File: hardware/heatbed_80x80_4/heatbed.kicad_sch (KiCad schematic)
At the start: 1 part, among them J1 PWR

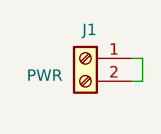
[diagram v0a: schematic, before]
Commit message: Increase holes' diameters
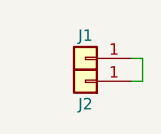
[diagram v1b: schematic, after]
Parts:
- removed J1: PWR, Connector_PinHeader_2.54mm:PinHeader_1x02_P2.54mm_Vertical, symbol Connector:Screw_Terminal_01x02
- added J1, J2: Conn_01x01, Connector_Pin:Pin_D1.3mm_L11.0mm, symbol Connector_Generic:Conn_01x01
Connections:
- new net: J1.1 (Pin_1), J2.1 (Pin_1)
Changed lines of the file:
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@@
     (stroke (width 0) (type default))
   )
-  (symbol (lib_id "Connector:Screw_Terminal_01x02") (at 147.32 100.33 0) (mirror y) (unit 1)
-    (in_bom yes) (on_board yes) (dnp no)
-    (property "Reference" "J1" (at 148.59 97.155 0)
-      (effects (font (size 1.27 1.27)) (justify left))
+  (symbol (lib_id "Connector_Generic:Conn_01x01") (at 147.32 100.33 180) (unit 1)
+    (in_bom yes) (on_board yes) (dnp no) (fields_autoplaced)
+    (property "Reference" "J1" (at 147.32 97.79 0)
+      (effects (font (size 1.27 1.27)))
     )
-    (property "Value" "PWR" (at 144.78 102.235 0)
-      (effects (font (size 1.27 1.27)) (justify left))
+    (property "Value" "Conn_01x01" (at 147.32 97.79 0)
+      (effects (font (size 1.27 1.27)) hide)
     )
-    (property "Footprint" "Connector_PinHeader_2.54mm:PinHeader_1x02_P2.54mm_Vertical" (at 147.32 100.33 0)
+    (property "Footprint" "Connector_Pin:Pin_D1.3mm_L11.0mm" (at 147.32 100.33 0)
       (effects (font (size 1.27 1.27)) hide)
     )
@@
     )
     (pin "1")
-    (pin "2")
     (instances
       (project "heatbed"
@@
         )
       )
+    )
+  )
+  (symbol (lib_id "Connector_Generic:Conn_01x01") (at 147.32 102.87 180) (unit 1)
+    (in_bom yes) (on_board yes) (dnp no)
+    (property "Reference" "J2" (at 147.32 105.41 0)
+      (effects (font (size 1.27 1.27)))
+    )
+    (property "Value" "Conn_01x01" (at 147.32 100.33 0)
+      (effects (font (size 1.27 1.27)) hide)
+    )
+    (property "Footprint" "Connector_Pin:Pin_D1.3mm_L11.0mm" (at 147.32 102.87 0)
+      (effects (font (size 1.27 1.27)) hide)
+    )
+    (property "Datasheet" "~" (at 147.32 102.87 0)
+      (effects (font (size 1.27 1.27)) hide)
+    )
+    (pin "1")
+    (instances
+      (project "heatbed"
+        (path "/f6f1e229-f102-463e-b32b-76ca65db5faf"
+          (reference "J2") (unit 1)
+        )
+      )
